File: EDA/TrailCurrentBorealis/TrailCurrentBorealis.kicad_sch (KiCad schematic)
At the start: 13 parts, among them IC1 SN65HVD230DR, J1 DHT22, J2 S4B-XH-SM4-TB, J3 CO2_IAQ, U1 ESP32-S3-Zero, U3 Mini560

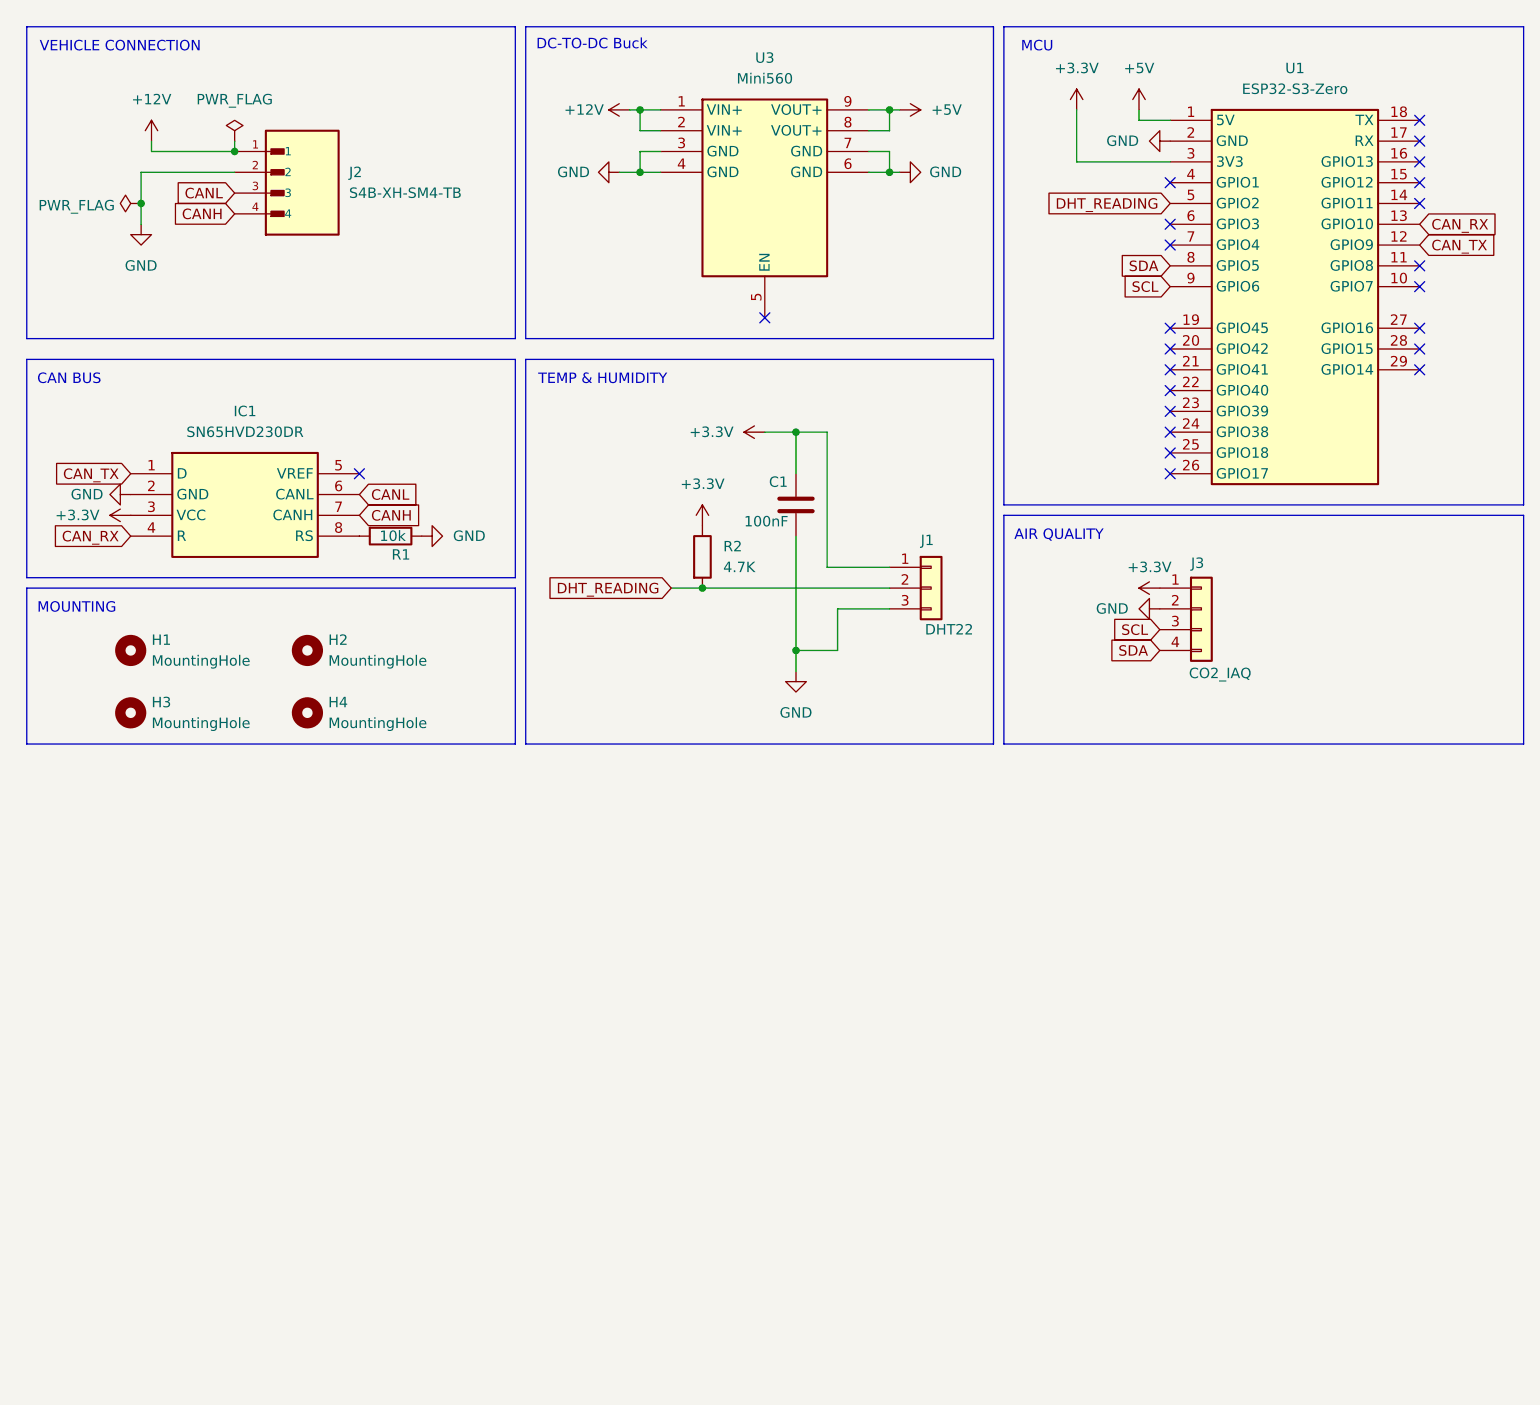
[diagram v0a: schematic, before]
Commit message: CAD for milling PCB on Genmistu 3030 just edges and drill holes not tracks
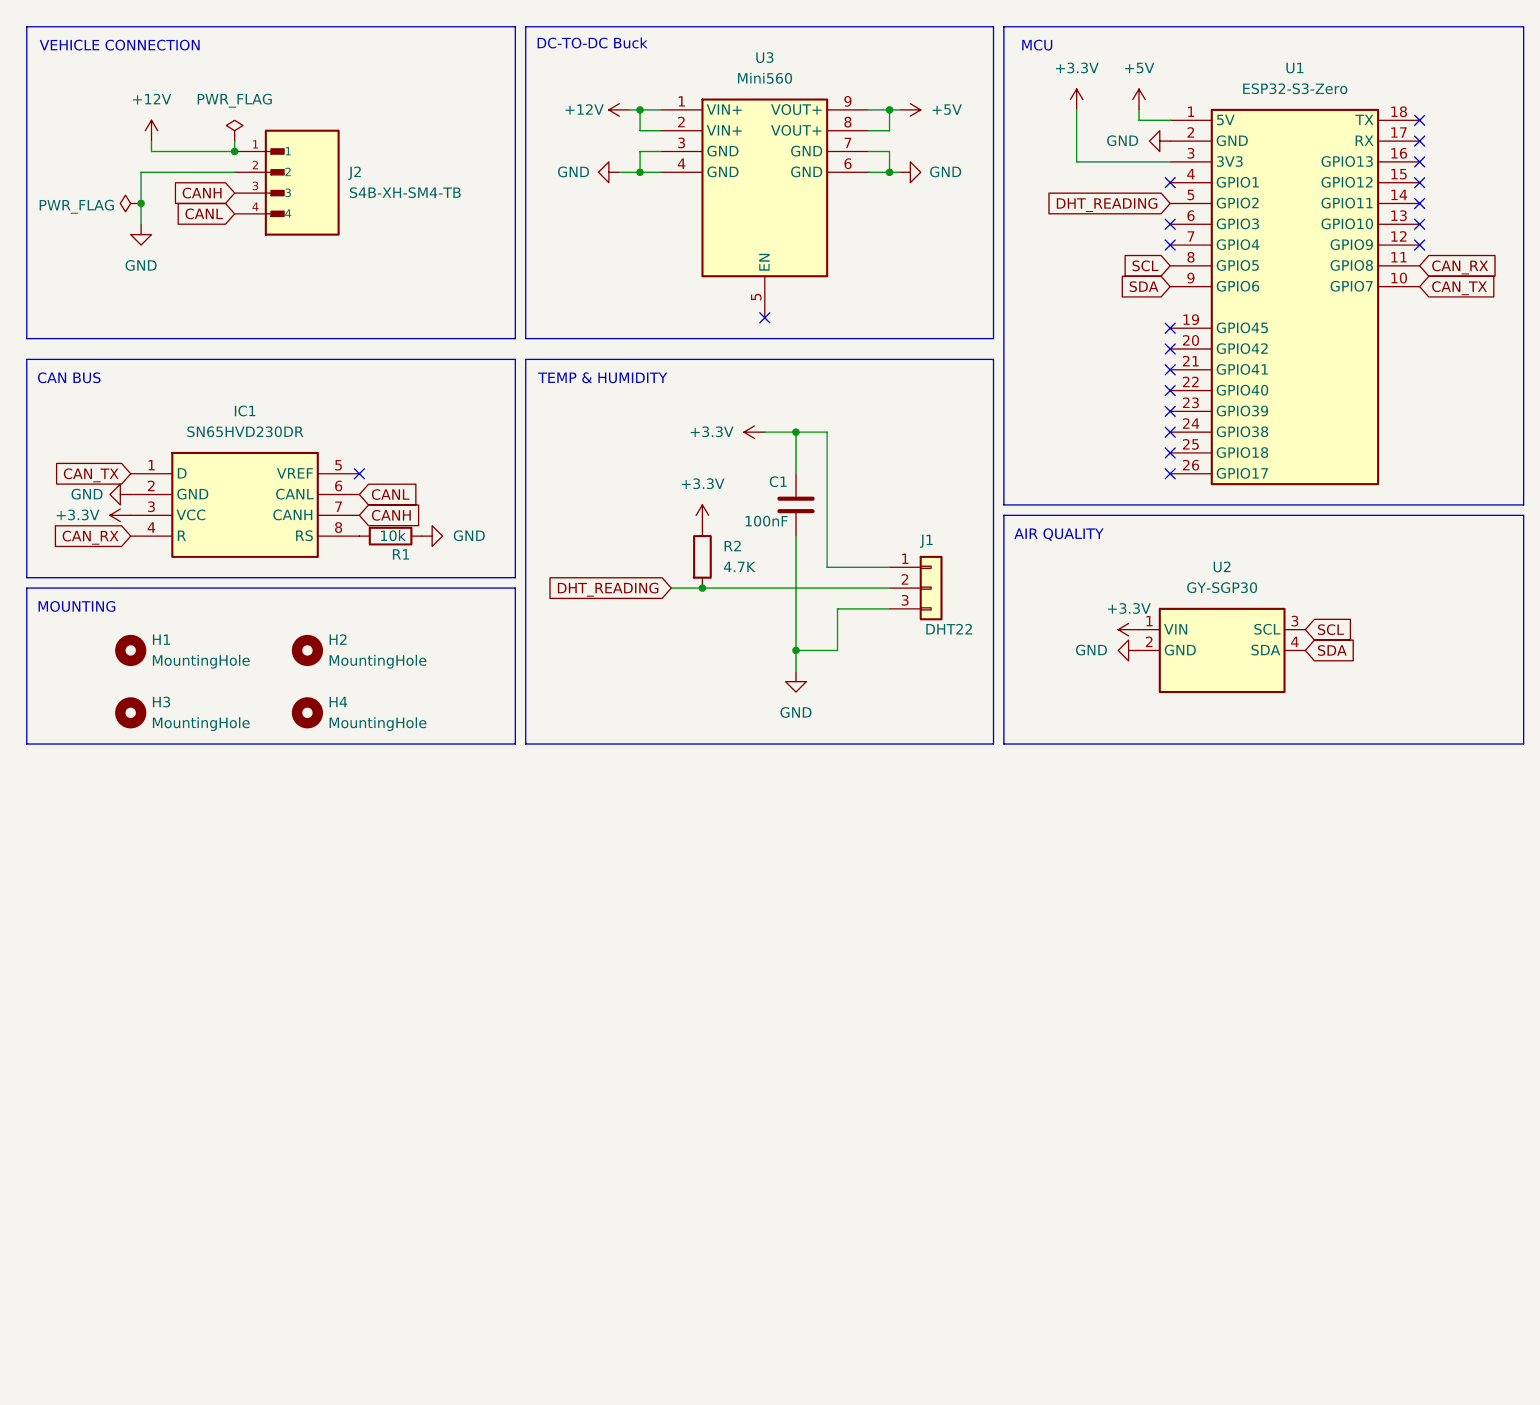
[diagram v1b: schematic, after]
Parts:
- removed J3: CO2_IAQ, Connector_PinSocket_2.54mm:PinSocket_1x04_P2.54mm_Horizontal, symbol Connector_Generic:Conn_01x04
- added U2: GY-SGP30, TrailCurrentFootprints:GY-SGP30, symbol TrailCurrentSymbolLibrary:GY-SGP30
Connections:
- net +3.3V: now also U2.1 (VIN)
- net CANH: now also J2.3; no longer J2.4
- net CANL: now also J2.4; no longer J2.3
- net CAN_RX: now also U1.11 (GPIO8); no longer U1.13 (GPIO10)
- net CAN_TX: now also U1.10 (GPIO7); no longer U1.12 (GPIO9)
- net GND: now also U2.2 (GND)
- net SCL: now also U1.8 (GPIO5), U2.3 (SCL); no longer U1.9 (GPIO6)
- net SDA: now also U1.9 (GPIO6), U2.4 (SDA); no longer U1.8 (GPIO5)
- no-connect marks 23 -> 20

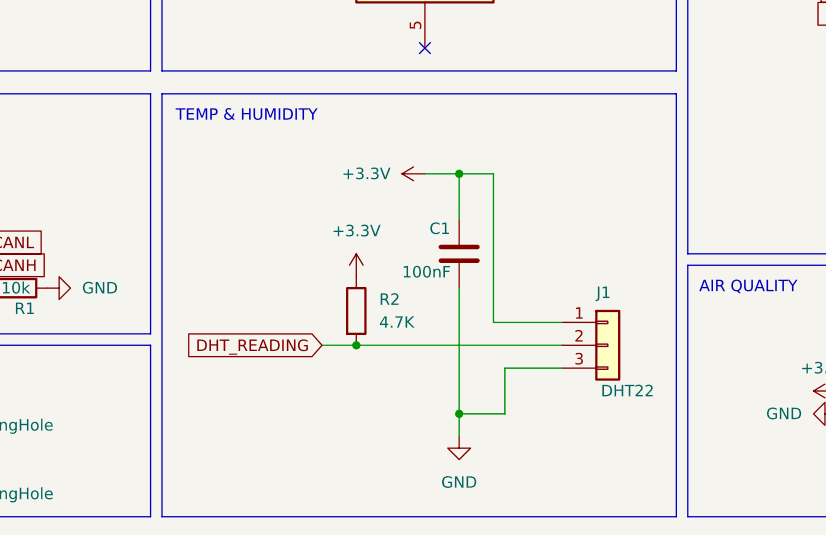
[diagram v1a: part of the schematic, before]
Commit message: Switching to new temp and humdity sensor
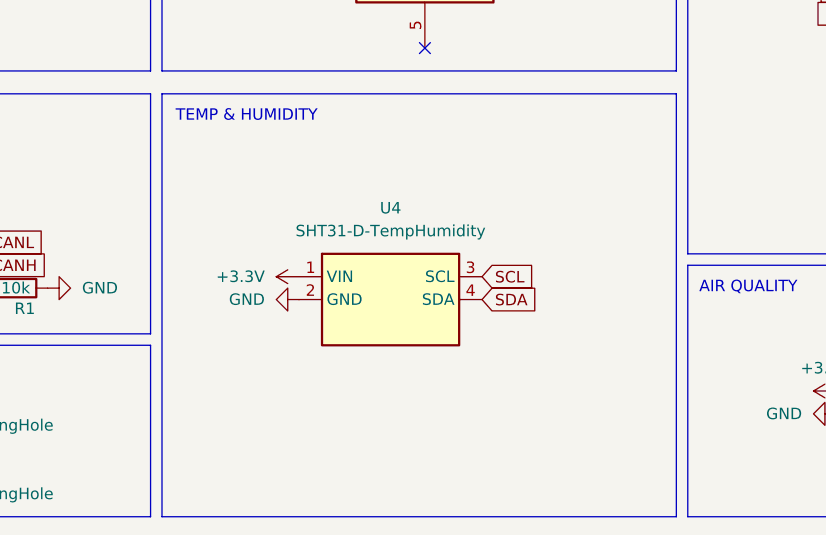
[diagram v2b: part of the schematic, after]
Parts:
- removed C1: 100nF, Capacitor_SMD:C_1206_3216Metric_Pad1.33x1.80mm_HandSolder, symbol Device:C
- removed J1: DHT22, Sensor:DHT22_Module, symbol Connector_Generic:Conn_01x03
- removed R2: 4.7K, Capacitor_SMD:C_1206_3216Metric_Pad1.33x1.80mm_HandSolder, symbol Device:R
- added U4: SHT31-D-TempHumidity, TrailCurrentFootprints:SHT31-D-TempHumidity, symbol TrailCurrentSymbolLibrary:SHT31-D-TempHumidity
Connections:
- net +3.3V: now also U4.1 (VIN)
- net GND: now also U4.2 (GND)
- net SCL: now also U4.3 (SCL)
- net SDA: now also U4.4 (SDA)

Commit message: Updated PCB for DIY build
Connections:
- net SCL: now also U1.9 (GPIO6); no longer U1.8 (GPIO5)
- net SDA: now also U1.8 (GPIO5); no longer U1.9 (GPIO6)

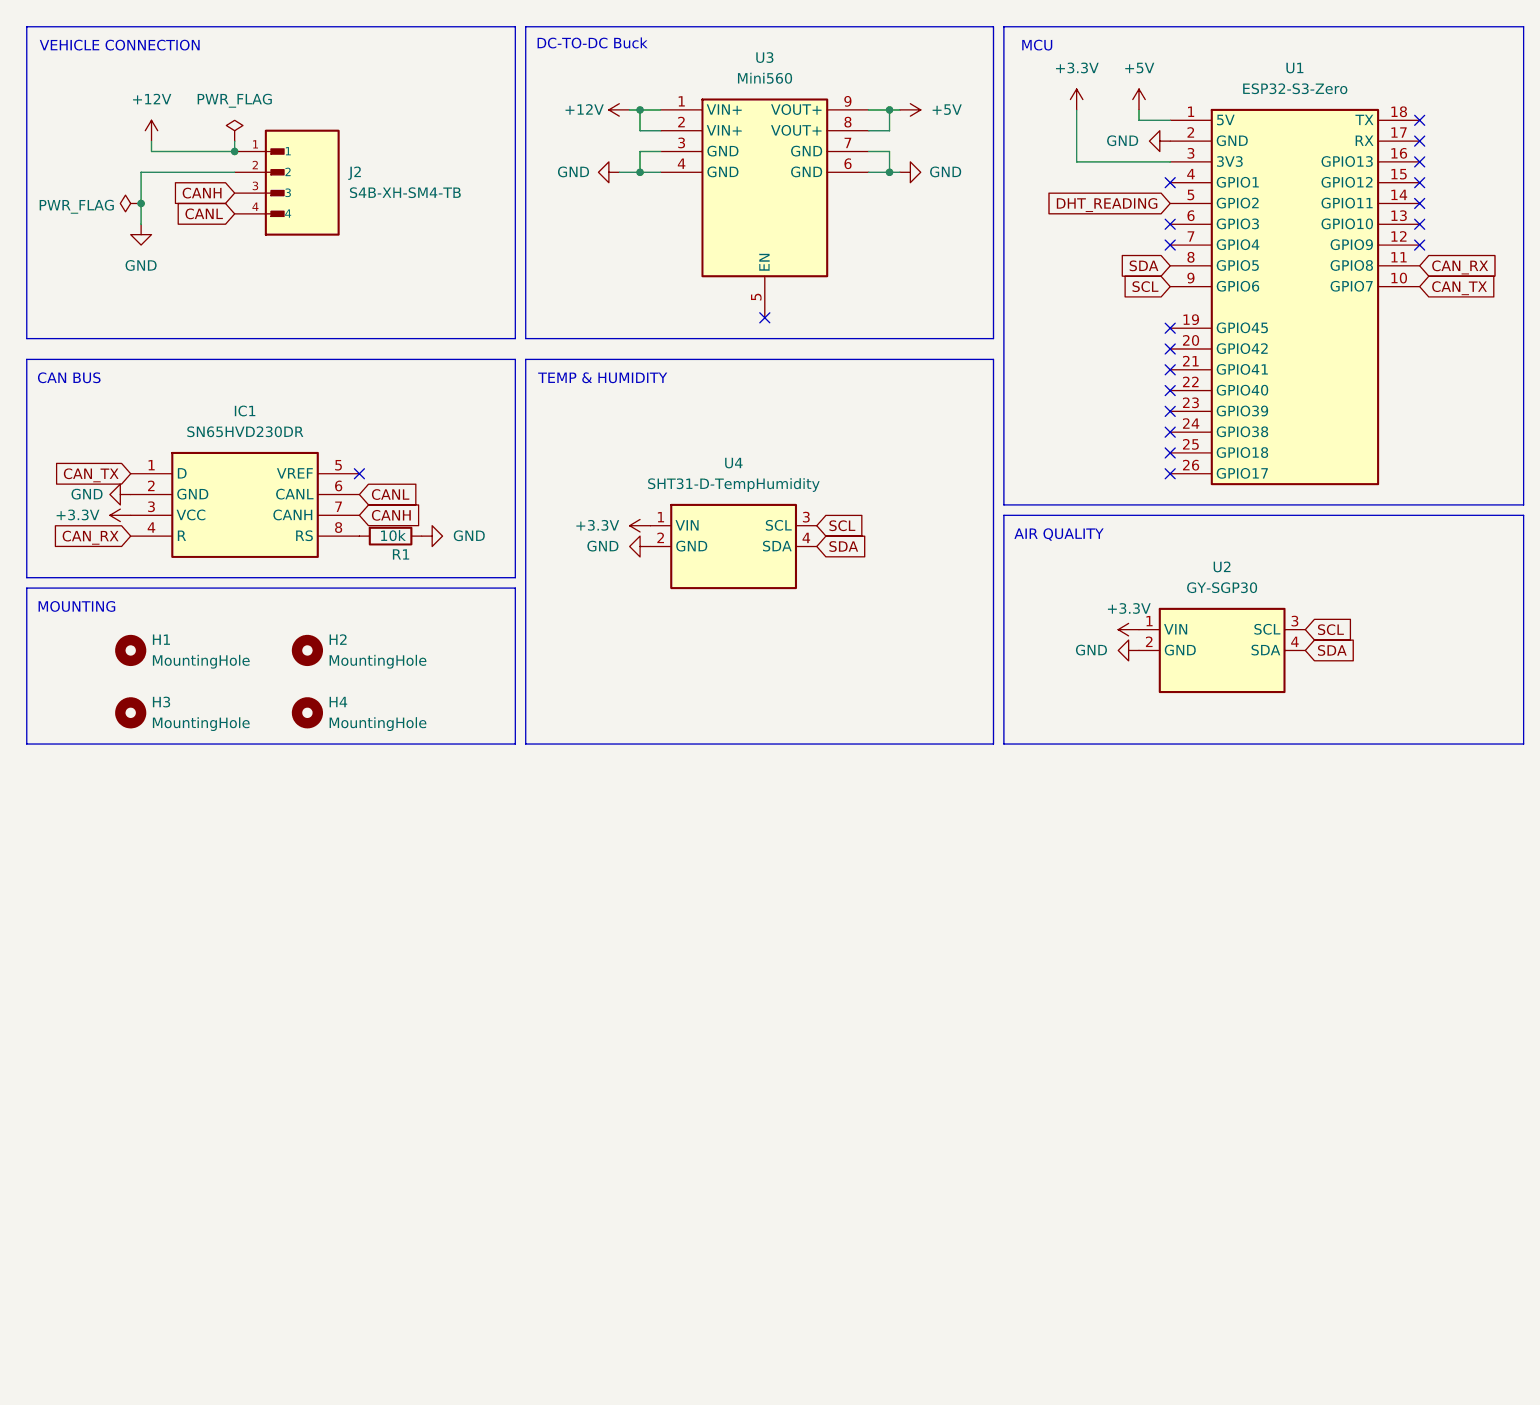
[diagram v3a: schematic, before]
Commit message: WIP EDA advancing the PCB further with better buck converter and reverse polarity protection
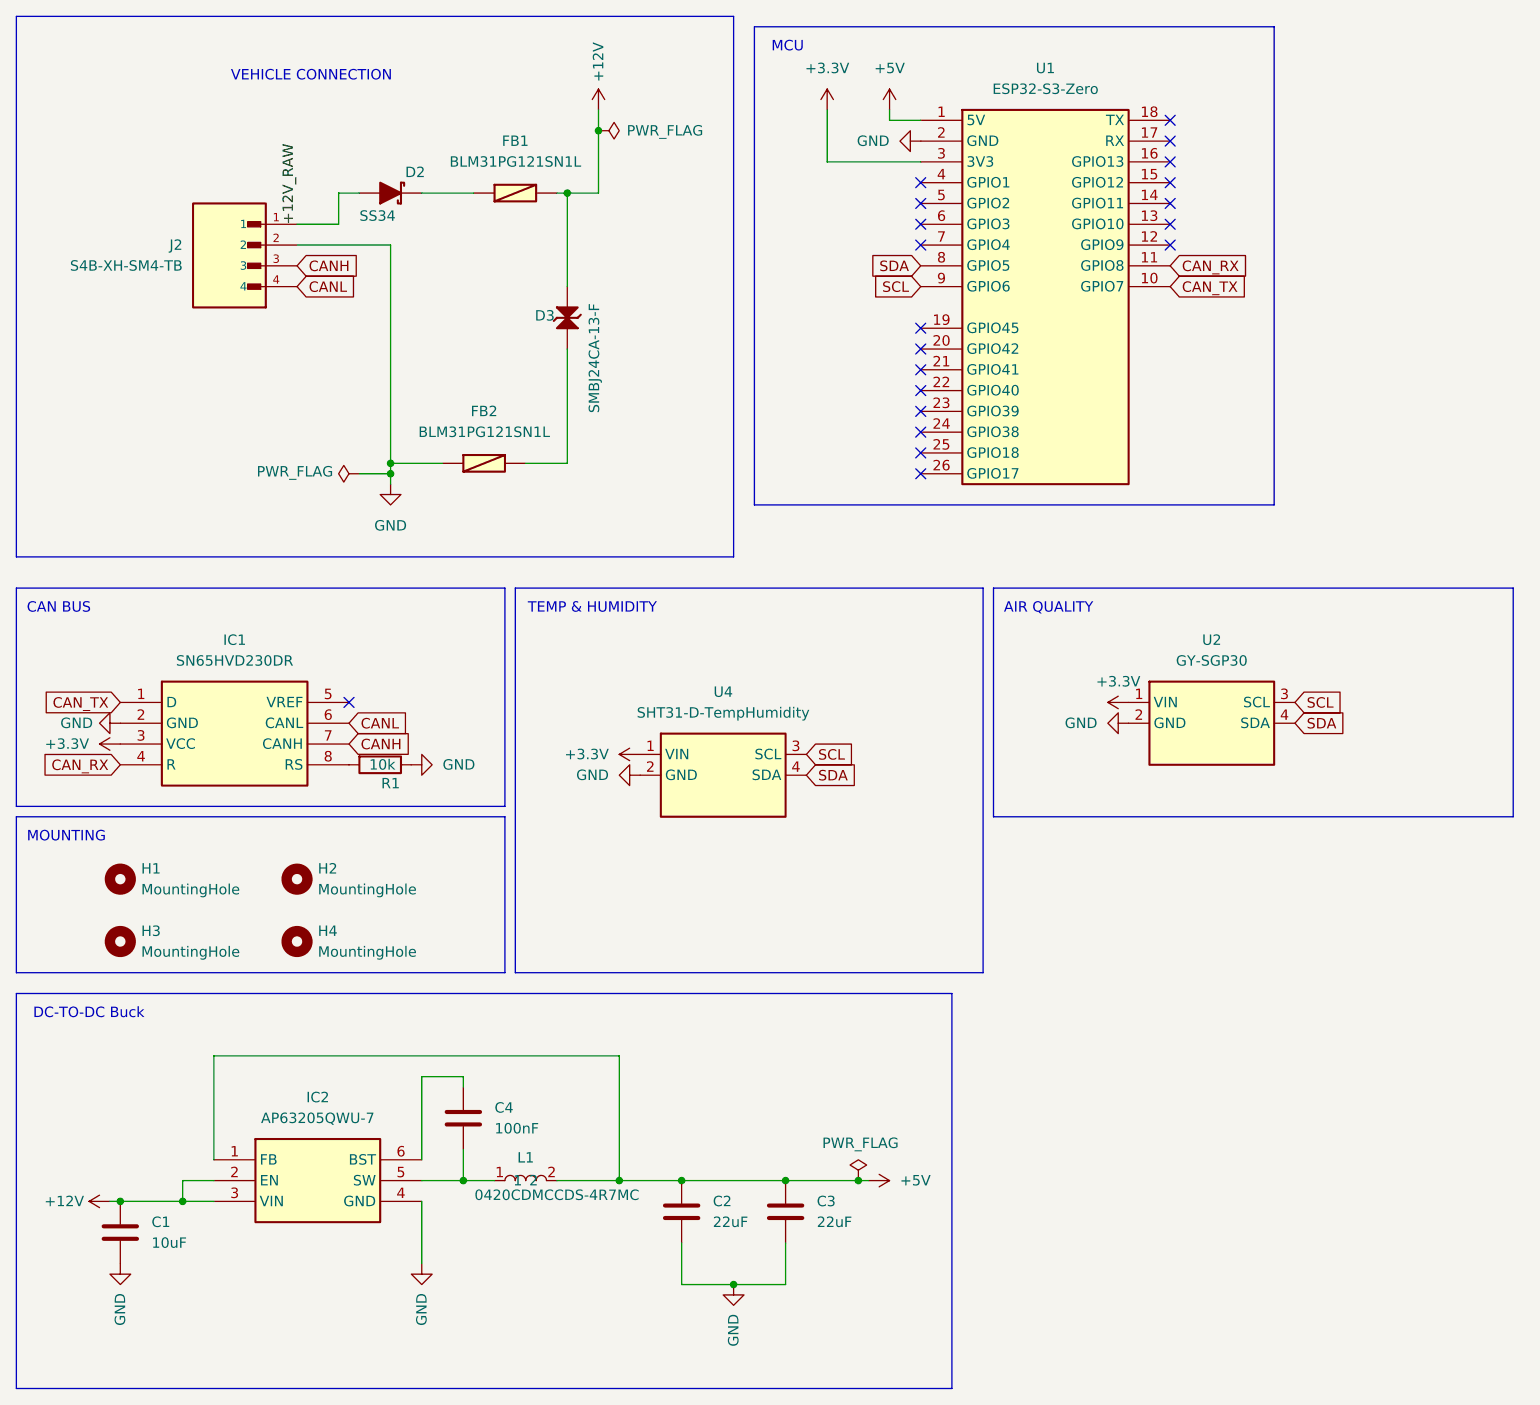
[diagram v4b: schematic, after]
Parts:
- removed U3: Mini560, TrailCurrentFootprints:Mini560, symbol TrailCurrentSymbolLibrary:Mini560
- added C1: 10uF, Capacitor_SMD:C_1206_3216Metric_Pad1.33x1.80mm_HandSolder, symbol Device:C
- added C2, C3: 22uF, Capacitor_SMD:C_1206_3216Metric_Pad1.33x1.80mm_HandSolder, symbol Device:C
- added C4: 100nF, Capacitor_SMD:C_1206_3216Metric_Pad1.33x1.80mm_HandSolder, symbol Device:C
- added D2: SS34, TrailCurrentFootprints:SS34, symbol TrailCurrentSymbolLibrary:SS34
- added D3: SMBJ24CA-13-F, TrailCurrentFootprints:SMBJ24CA-13-F, symbol TrailCurrentSymbolLibrary:SMBJ24CA-13-F
- added FB1, FB2: BLM31PG121SN1L, TrailCurrentFootprints:BLM31PG121SN1L, symbol TrailCurrentSymbolLibrary:BLM31PG121SN1L
- added IC2: AP63205QWU-7, TrailCurrentFootprints:AP63205QWU7, symbol TrailCurrentSymbolLibrary:AP63205QWU-7
- added L1: 0420CDMCCDS-4R7MC, TrailCurrentFootprints:0420CDMCCDS-4R7MC, symbol TrailCurrentSymbolLibrary:0420CDMCCDS-4R7MC
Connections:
- net +12V: now also C1.1, D3.2, FB1.2, IC2.2 (EN), IC2.3 (VIN); no longer J2.1
- net +5V: now also C2.1, C3.1, IC2.1 (FB), L1.2
- net GND: now also C1.2, C2.2, C3.2, FB2.1, IC2.4 (GND)
- net DHT_READING: no longer names the net of U1.5 (GPIO2)
- new net: D3.1, FB2.2
- new net: C4.2, IC2.5 (SW), L1.1
- new net: D2.1 (K), FB1.1
- new net: C4.1, IC2.6 (BST)
- new net +12V_RAW: D2.2 (A), J2.1
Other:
- moved on the sheet: H1, H2, H3, H4, IC1, J2, R1, U1, U2, U4
